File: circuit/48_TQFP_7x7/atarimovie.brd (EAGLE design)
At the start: 72.4 x 82.5 mm, 24 parts, among them IC1 AMS1117-3.3V, J1 CARTRIDGE EDGE, J2 TF-15X15, U1 DSPIC33CKXXMC105-X_M4TQFP48_7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, U2 74LVCH245APW,118, U3 74LVCH245APW,118, X1 22-23-2051

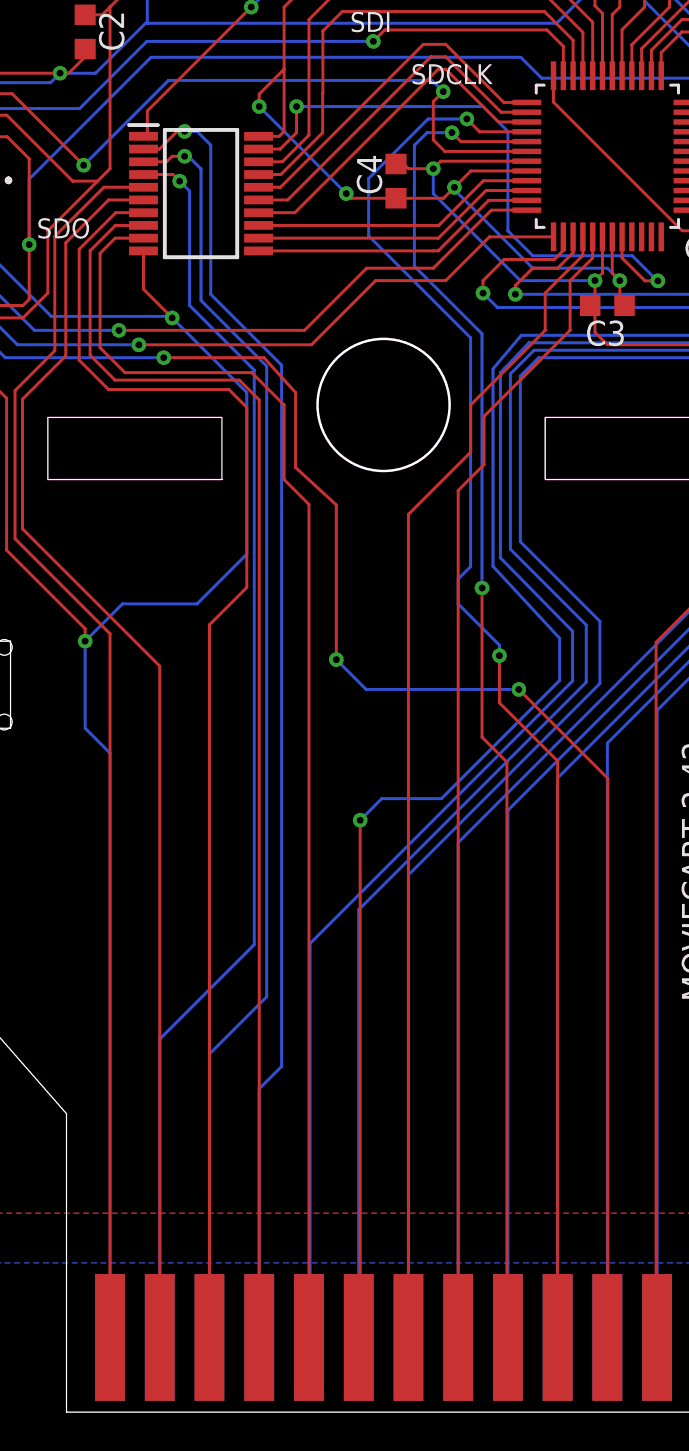
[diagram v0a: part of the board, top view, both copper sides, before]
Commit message: gerber files and rerouting away from post hole slightly
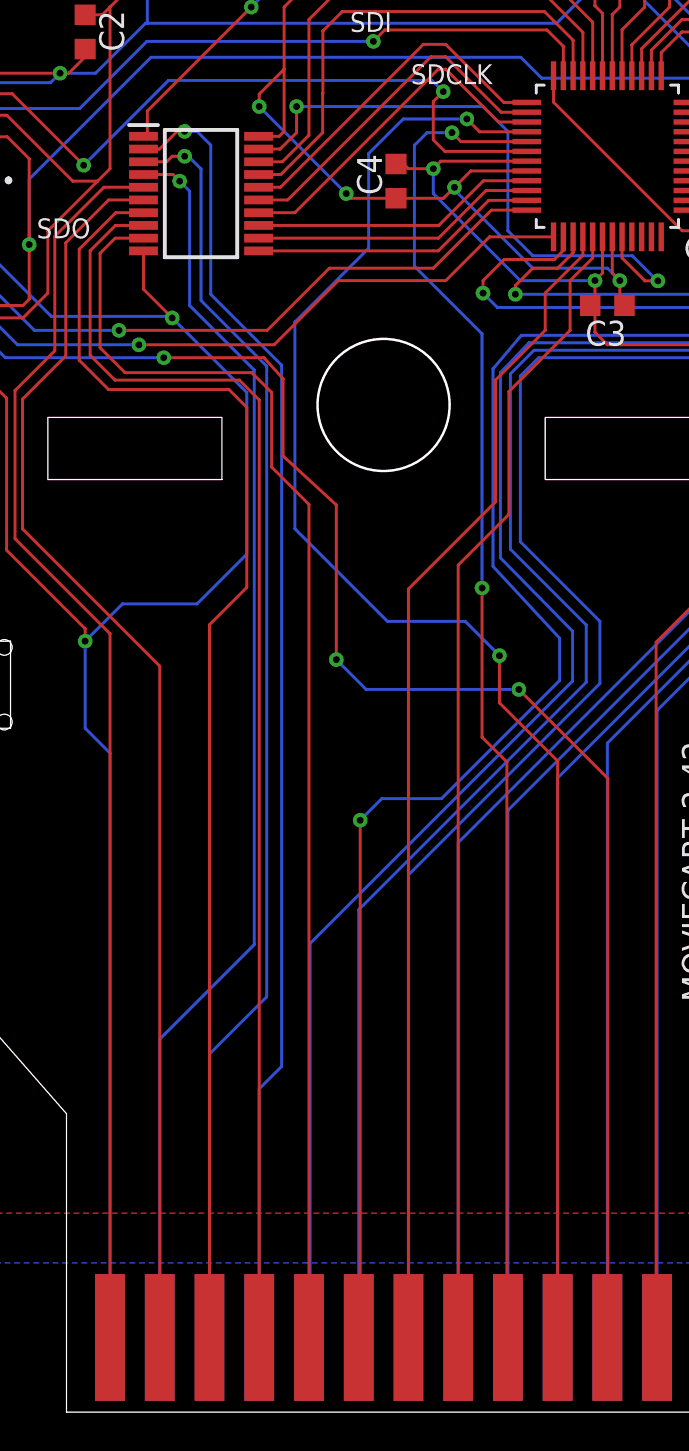
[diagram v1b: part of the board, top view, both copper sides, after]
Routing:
- net CADDR8: track 73.3 -> 79.0 mm
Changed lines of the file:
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@@
 <wire x1="42.7482" y1="38.6334" x2="42.7482" y2="36.2204" width="0.1524" layer="1"/>
 <wire x1="45.72" y1="3.81" x2="45.72" y2="33.2486" width="0.1524" layer="1"/>
-<wire x1="41.0845" y1="66.04" x2="39.1033" y2="66.04" width="0.1524" layer="16"/>
+<wire x1="41.0845" y1="66.04" x2="37.8333" y2="66.04" width="0.1524" layer="16"/>
 <via x="42.7482" y="38.6334" extent="1-16" drill="0.35"/>
-<wire x1="36.068" y1="60.071" x2="36.068" y2="63.0047" width="0.1524" layer="16"/>
-<wire x1="39.1033" y1="66.04" x2="36.068" y2="63.0047" width="0.1524" layer="16"/>
-<wire x1="41.275" y1="54.864" x2="36.068" y2="60.071" width="0.1524" layer="16"/>
+<wire x1="36.068" y1="59.436" x2="32.3013" y2="55.6693" width="0.1524" layer="16"/>
+<wire x1="36.068" y1="59.436" x2="36.068" y2="64.2747" width="0.1524" layer="16"/>
+<wire x1="37.8333" y1="66.04" x2="36.068" y2="64.2747" width="0.1524" layer="16"/>
 <wire x1="44.1452" y1="65.385" x2="41.7395" y2="65.385" width="0.1524" layer="1"/>
 <wire x1="41.7395" y1="65.385" x2="41.0845" y2="66.04" width="0.1524" layer="1"/>
-<wire x1="41.275" y1="54.864" x2="41.275" y2="43.18" width="0.1524" layer="16"/>
-<wire x1="41.275" y1="43.18" x2="40.64" y2="42.545" width="0.1524" layer="16"/>
-<wire x1="40.64" y1="42.545" x2="40.64" y2="41.275" width="0.1524" layer="16"/>
-<wire x1="42.7482" y1="38.6334" x2="42.7482" y2="39.1668" width="0.1524" layer="16"/>
-<wire x1="42.7482" y1="39.1668" x2="40.64" y2="41.275" width="0.1524" layer="16"/>
+<wire x1="42.7482" y1="38.6334" x2="40.99935" y2="40.38225" width="0.1524" layer="16"/>
+<wire x1="40.99935" y1="40.38225" x2="37.0332" y2="40.38225" width="0.1524" layer="16"/>
+<wire x1="32.3013" y1="45.11415" x2="32.3013" y2="55.6693" width="0.1524" layer="16"/>
+<wire x1="37.0332" y1="40.38225" x2="32.3013" y2="45.11415" width="0.1524" layer="16"/>
 </signal>
 <signal name="CADDR9">
@@
 <contactref element="U1" pad="40"/>
 <wire x1="45.085" y1="57.15" x2="45.085" y2="55.245" width="0.1524" layer="1"/>
-<wire x1="38.1" y1="3.81" x2="38.1" y2="45.847" width="0.1524" layer="1"/>
-<wire x1="38.1" y1="45.847" x2="41.275" y2="49.022" width="0.1524" layer="1"/>
-<wire x1="41.275" y1="49.022" x2="41.275" y2="51.435" width="0.1524" layer="1"/>
-<wire x1="45.085" y1="55.245" x2="41.275" y2="51.435" width="0.1524" layer="1"/>
+<wire x1="38.1" y1="3.81" x2="38.1" y2="42.037" width="0.1524" layer="1"/>
+<wire x1="38.1" y1="42.037" x2="42.545" y2="46.482" width="0.1524" layer="1"/>
+<wire x1="42.545" y1="46.482" x2="42.545" y2="52.705" width="0.1524" layer="1"/>
+<wire x1="45.085" y1="55.245" x2="42.545" y2="52.705" width="0.1524" layer="1"/>
 <wire x1="47.01" y1="60.0202" x2="47.01" y2="59.075" width="0.1524" layer="1"/>
 <wire x1="47.01" y1="59.075" x2="45.085" y2="57.15" width="0.1524" layer="1"/>
@@
 <contactref element="U1" pad="36"/>
 <contactref element="X1" pad="4"/>
-<wire x1="32.7914" y1="55.245" x2="23.3172" y2="55.245" width="0.1524" layer="1"/>
-<wire x1="35.9664" y1="58.42" x2="32.7914" y2="55.245" width="0.1524" layer="1"/>
+<wire x1="30.8864" y1="55.245" x2="23.3172" y2="55.245" width="0.1524" layer="1"/>
+<wire x1="34.0614" y1="58.42" x2="30.8864" y2="55.245" width="0.1524" layer="1"/>
 <via x="23.3172" y="55.245" extent="1-16" drill="0.35"/>
 <wire x1="23.3172" y1="55.245" x2="18.9992" y2="55.245" width="0.1524" layer="16"/>
 <wire x1="7.62" y1="78.74" x2="7.62" y2="66.6242" width="0.1524" layer="16"/>
 <wire x1="7.62" y1="66.6242" x2="18.9992" y2="55.245" width="0.1524" layer="16"/>
-<wire x1="39.37" y1="58.42" x2="35.9664" y2="58.42" width="0.1524" layer="1"/>
+<wire x1="39.37" y1="58.42" x2="34.0614" y2="58.42" width="0.1524" layer="1"/>
 <wire x1="44.1452" y1="61.385" x2="42.335" y2="61.385" width="0.1524" layer="1"/>
 <wire x1="42.335" y1="61.385" x2="39.37" y2="58.42" width="0.1524" layer="1"/>
@@
 <contactref element="X1" pad="5"/>
 <contactref element="U1" pad="37"/>
-<wire x1="24.3332" y1="54.5084" x2="33.147" y2="54.5084" width="0.1524" layer="1"/>
+<wire x1="24.3332" y1="54.5084" x2="31.242" y2="54.5084" width="0.1524" layer="1"/>
 <via x="24.3332" y="54.5084" extent="1-16" drill="0.35"/>
-<wire x1="36.4236" y1="57.785" x2="40.005" y2="57.785" width="0.1524" layer="1"/>
-<wire x1="33.147" y1="54.5084" x2="36.4236" y2="57.785" width="0.1524" layer="1"/>
+<wire x1="34.5186" y1="57.785" x2="40.005" y2="57.785" width="0.1524" layer="1"/>
+<wire x1="31.242" y1="54.5084" x2="34.5186" y2="57.785" width="0.1524" layer="1"/>
 <wire x1="5.08" y1="78.74" x2="3.7465" y2="77.4065" width="0.1524" layer="16"/>
 <wire x1="3.7465" y1="68.8975" x2="3.7465" y2="77.4065" width="0.1524" layer="16"/>
@@
 <contactref element="U1" pad="41"/>
 <wire x1="46.355" y1="57.785" x2="46.355" y2="55.245" width="0.1524" layer="1"/>
-<wire x1="40.64" y1="47.06694375" x2="40.64" y2="3.81" width="0.1524" layer="1"/>
-<wire x1="41.9608" y1="50.8508" x2="41.9608" y2="48.38774375" width="0.1524" layer="1"/>
-<wire x1="46.355" y1="55.245" x2="41.9608" y2="50.8508" width="0.1524" layer="1"/>
-<wire x1="41.9608" y1="48.38774375" x2="40.64" y2="47.06694375" width="0.1524" layer="1"/>
+<wire x1="40.64" y1="43.25694375" x2="40.64" y2="3.81" width="0.1524" layer="1"/>
+<wire x1="43.2308" y1="52.1208" x2="43.2308" y2="45.84774375" width="0.1524" layer="1"/>
+<wire x1="46.355" y1="55.245" x2="43.2308" y2="52.1208" width="0.1524" layer="1"/>
+<wire x1="43.2308" y1="45.84774375" x2="40.64" y2="43.25694375" width="0.1524" layer="1"/>
 <wire x1="47.51" y1="60.0202" x2="47.51" y2="58.94" width="0.1524" layer="1"/>
 <wire x1="47.51" y1="58.94" x2="46.355" y2="57.785" width="0.1524" layer="1"/>
@@
 <wire x1="22.352" y1="54.356" x2="23.622" y2="53.086" width="0.1524" layer="1"/>
 <wire x1="23.622" y1="53.086" x2="30.099" y2="53.086" width="0.1524" layer="1"/>
-<wire x1="30.099" y1="53.086" x2="31.75" y2="51.435" width="0.1524" layer="1"/>
-<wire x1="31.75" y1="47.625" x2="33.02" y2="46.355" width="0.1524" layer="1"/>
-<wire x1="31.75" y1="51.435" x2="31.75" y2="47.625" width="0.1524" layer="1"/>
+<wire x1="30.099" y1="53.086" x2="31.115" y2="52.07" width="0.1524" layer="1"/>
+<wire x1="31.115" y1="48.26" x2="33.02" y2="46.355" width="0.1524" layer="1"/>
+<wire x1="31.115" y1="52.07" x2="31.115" y2="48.26" width="0.1524" layer="1"/>
 <wire x1="33.02" y1="46.355" x2="33.02" y2="3.81" width="0.1524" layer="1"/>
 <wire x1="24.5702" y1="59.95339375" x2="23.12339375" y2="59.95339375" width="0.1524" layer="1"/>
@@
 <via x="43.7388" y="36.9062" extent="1-16" drill="0.35"/>
 <wire x1="25.6032" y1="53.848" x2="30.7213" y2="53.848" width="0.1524" layer="1"/>
-<wire x1="30.7213" y1="53.848" x2="32.3342" y2="52.07" width="0.1524" layer="1"/>
-<wire x1="32.3342" y1="52.07" x2="32.3342" y2="48.2441625" width="0.1524" layer="1"/>
-<wire x1="32.3342" y1="48.2441625" x2="34.417" y2="46.3264625" width="0.1524" layer="1"/>
+<wire x1="30.7213" y1="53.848" x2="31.6992" y2="52.77" width="0.1524" layer="1"/>
+<wire x1="31.6992" y1="52.77" x2="31.6992" y2="48.828828125" width="0.1524" layer="1"/>
+<wire x1="31.6992" y1="48.828828125" x2="34.417" y2="46.3264625" width="0.1524" layer="1"/>
 <wire x1="34.417" y1="46.3264625" x2="34.417" y2="38.4302" width="0.1524" layer="1"/>
 <contactref element="IC1" pad="3"/>

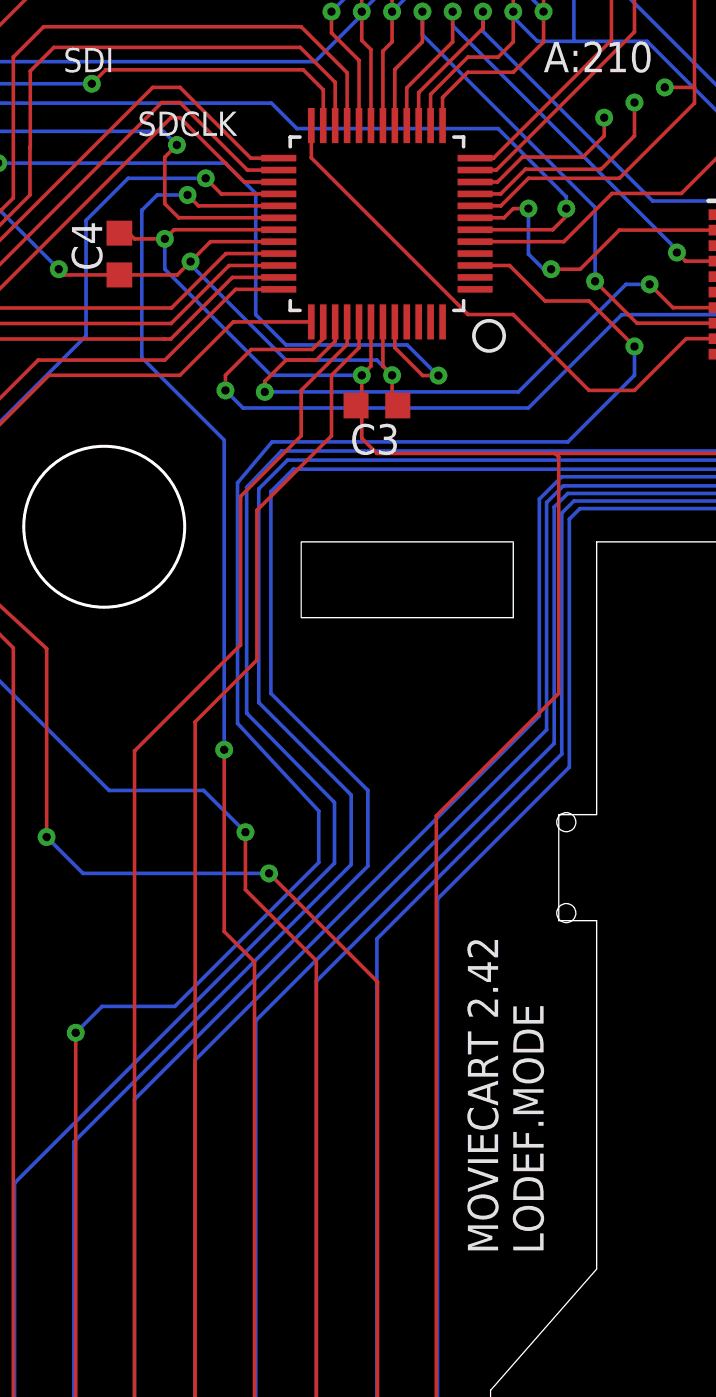
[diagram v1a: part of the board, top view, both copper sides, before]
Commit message: spaced out caddr8 caddr9 @LODEFMODE not LODEF.MODE
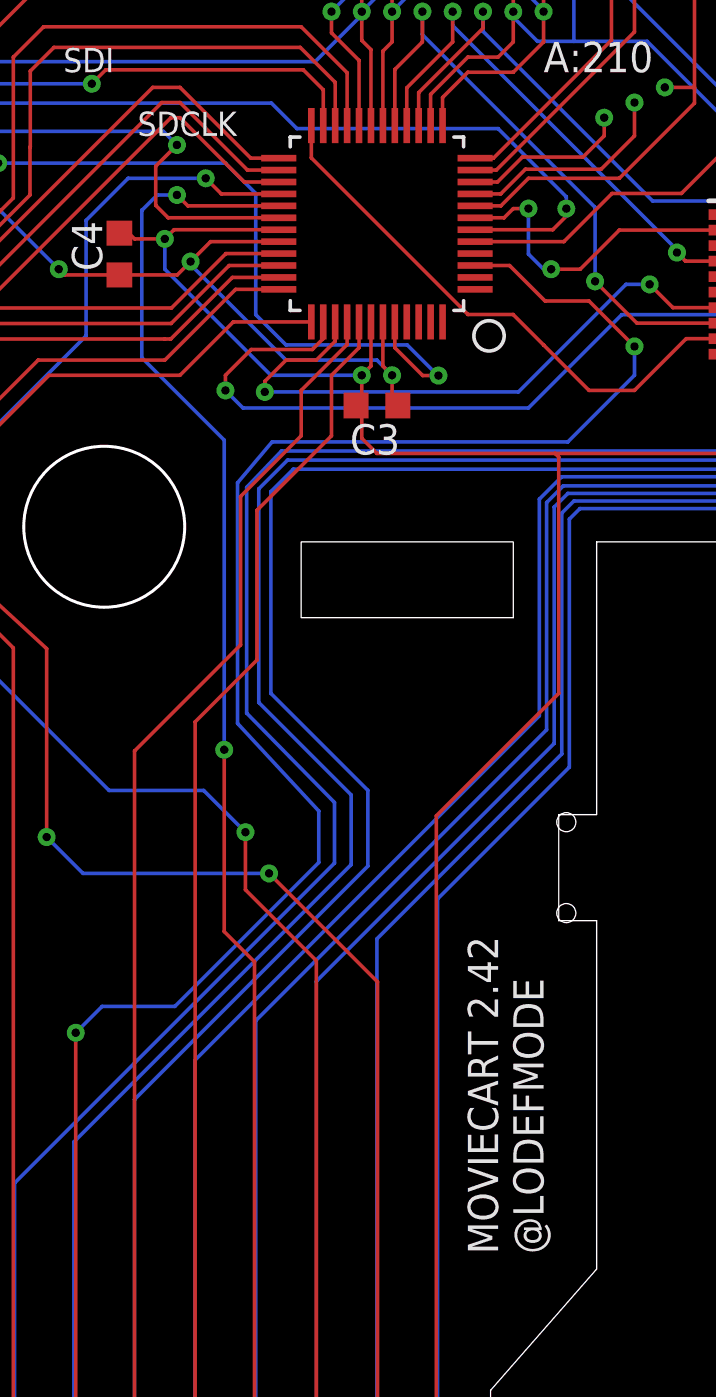
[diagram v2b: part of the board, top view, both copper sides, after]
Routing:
- net SDCLK: track 34.6 -> 35.2 mm
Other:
- board text added: "@LODEFMODE"
- board text removed: "LODEF.MODE"
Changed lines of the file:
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@@
 <text x="56.0705" y="75.2475" size="1.016" layer="25">SDCS</text>
 <text x="19.1135" y="59.944" size="1.016" layer="25">SDO</text>
-<text x="55.245" y="20.955" size="1.27" layer="21" font="vector" rot="R90">LODEF.MODE</text>
+<text x="55.245" y="20.955" size="1.27" layer="21" font="vector" rot="R90">@LODEFMODE</text>
 </plain>
 <attributes>
@@
 <contactref element="J1" pad="21"/>
 <contactref element="U1" pad="29"/>
-<via x="40.3225" y="65.3415" extent="1-16" drill="0.35"/>
+<via x="39.878" y="65.3415" extent="1-16" drill="0.35"/>
 <wire x1="38.4048" y1="64.7065" x2="38.4048" y2="58.5216" width="0.1524" layer="16"/>
 <wire x1="39.0525" y1="65.3415" x2="38.4175" y2="64.7065" width="0.1524" layer="16"/>
-<wire x1="39.0525" y1="65.3415" x2="40.3225" y2="65.3415" width="0.1524" layer="16"/>
+<wire x1="39.0525" y1="65.3415" x2="39.878" y2="65.3415" width="0.1524" layer="16"/>
 <wire x1="38.4175" y1="64.7065" x2="38.4048" y2="64.7065" width="0.1524" layer="16"/>
 <wire x1="43.18" y1="3.81" x2="43.1292" y2="3.81" width="0.1524" layer="1"/>
@@
 <wire x1="41.8592" y1="34.4678" x2="41.8592" y2="42.0878" width="0.1524" layer="1"/>
 <wire x1="43.1292" y1="3.81" x2="43.1292" y2="33.1978" width="0.1524" layer="1"/>
-<wire x1="44.1452" y1="64.885" x2="40.779" y2="64.885" width="0.1524" layer="1"/>
-<wire x1="40.779" y1="64.885" x2="40.3225" y2="65.3415" width="0.1524" layer="1"/>
+<wire x1="44.1452" y1="64.885" x2="40.3345" y2="64.885" width="0.1524" layer="1"/>
+<wire x1="40.3345" y1="64.885" x2="39.878" y2="65.3415" width="0.1524" layer="1"/>
 <wire x1="41.8592" y1="55.0672" x2="41.8592" y2="42.0878" width="0.1524" layer="16"/>
 <wire x1="38.4048" y1="58.5216" x2="41.8592" y2="55.0672" width="0.1524" layer="16"/>
@@
 <wire x1="39.3065" y1="68.0085" x2="39.878" y2="67.437" width="0.1524" layer="16"/>
 <wire x1="39.3065" y1="68.0085" x2="25.8445" y2="68.0085" width="0.1524" layer="16"/>
-<wire x1="39.37" y1="66.929" x2="39.878" y2="67.437" width="0.1524" layer="1"/>
-<wire x1="39.37" y1="64.97" x2="39.37" y2="66.929" width="0.1524" layer="1"/>
-<wire x1="44.1452" y1="64.385" x2="39.955" y2="64.385" width="0.1524" layer="1"/>
-<wire x1="39.955" y1="64.385" x2="39.37" y2="64.97" width="0.1524" layer="1"/>
+<wire x1="38.989" y1="66.548" x2="39.878" y2="67.437" width="0.1524" layer="1"/>
+<wire x1="38.989" y1="64.9065" x2="38.989" y2="66.548" width="0.1524" layer="1"/>
+<wire x1="44.1452" y1="64.385" x2="39.5105" y2="64.385" width="0.1524" layer="1"/>
+<wire x1="39.5105" y1="64.385" x2="38.989" y2="64.9065" width="0.1524" layer="1"/>
 </signal>
 <signal name="SDO">
